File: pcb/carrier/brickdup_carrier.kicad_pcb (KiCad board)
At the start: 2 copper layers, 62 x 44 mm, 33 parts, among them J1 VBAT IN (JST PH), SW1 PWR SWITCH (JST PH), U1 MP9486A

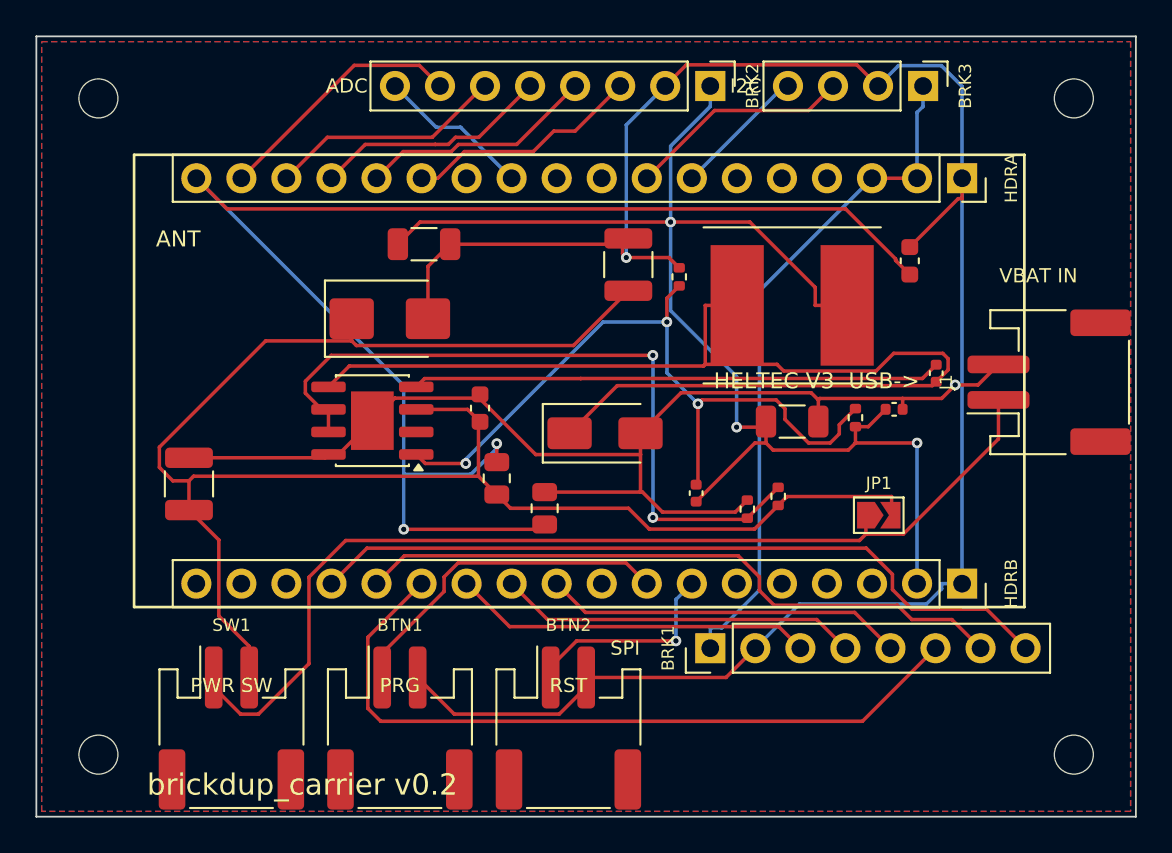
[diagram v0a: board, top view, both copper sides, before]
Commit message: pcb: widen carrier connector spacing for SMT assembly margins
Measured envelope gaps (pads+courtyard union) and widened the tight spots:
BTN1/BTN2 JST spacing 0.25mm -> 0.75mm courtyard gap, BRK1 moved 0.7mm south
of the HDRB socket. All machine-placed (SMT-SMT) pairs now >= 0.75mm; the
v0.1 D2 trouble cluster sits at D2<->D1 4.9mm / D2<->L1 13.9mm.

apply_route.py: WriteDRCReport crashes standalone; starved-thermal healing
moved to fix_thermals.py driven by kicad-cli DRC json. Final DRC: 0/0.

Co-Authored-By: Claude Fable 5 <noreply@anthropic.com>
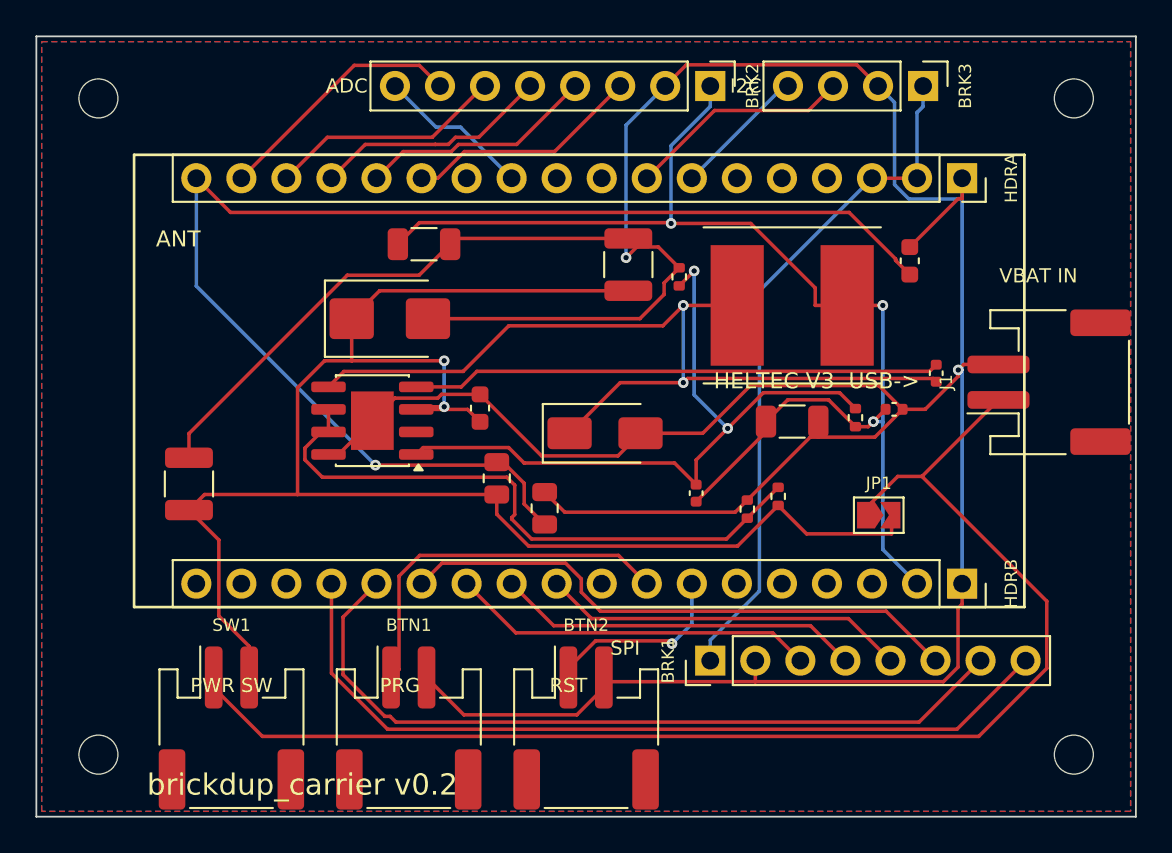
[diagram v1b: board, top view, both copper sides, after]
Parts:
- moved BTN2 1.00 mm to (31.0, 39.0)
- moved BRK1 0.70 mm to (38.0, 35.2)
- moved BTN1 0.50 mm to (21.0, 39.0)
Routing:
- net GND: track 185.0 -> 219.2 mm
- net VBATIN: track 58.0 -> 74.4 mm
- net SW: track 64.7 -> 51.3 mm, vias 0 -> 2
- net IO47: track 42.3 -> 32.2 mm
- net SENSE: track 82.4 -> 74.6 mm, vias 2 -> 1
- net +5V: track 78.2 -> 70.5 mm
- net IO48: track 37.3 -> 44.4 mm
- net EN: track 40.8 -> 34.7 mm, vias 2 -> 0
- net IO26: track 42.8 -> 47.1 mm
- net PRG: track 19.4 -> 21.0 mm
- net FB: track 41.5 -> 40.0 mm, vias 3 -> 2
- net RST: track 11.9 -> 10.9 mm
- net VBAT: track 96.9 -> 97.0 mm, vias 0 -> 2

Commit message: pcb: carrier Cff footprint 0402 -> 0603 for hand-rework
Cff is the designated bench-tuning part (hysteretic ripple injection); 0603
matches the cap kit and human hands. Re-placed + re-routed, DRC 0/0.

Co-Authored-By: Claude Fable 5 <noreply@anthropic.com>
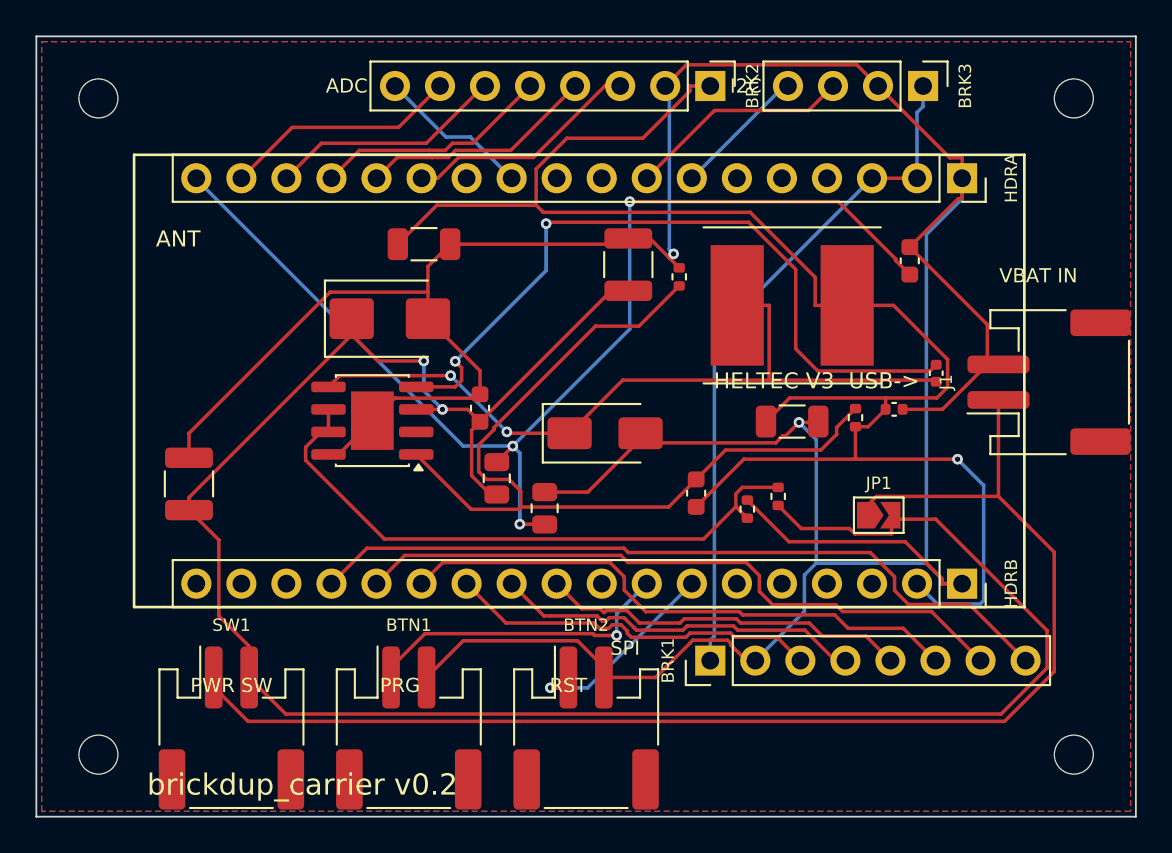
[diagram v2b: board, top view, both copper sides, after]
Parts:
- removed the Cff at (37.2, 25.8)
- added Cff: 470pF, C_0603_1608Metric, F.Cu at (37.2, 25.8)
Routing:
- net +5V: track 70.5 -> 96.4 mm, vias 3 -> 1
- net VBAT: track 97.0 -> 122.2 mm
- net GND: track 219.2 -> 203.2 mm
- net BST: track 29.8 -> 42.1 mm, vias 0 -> 2
- net SENSE: track 74.6 -> 65.4 mm, vias 1 -> 3
- net FB: track 40.0 -> 48.9 mm, vias 2 -> 0
- net SW: track 51.3 -> 43.2 mm
- net IO48: track 44.4 -> 37.7 mm
- net IO26: track 47.1 -> 43.0 mm
- net PRG: track 21.0 -> 17.7 mm, vias 0 -> 1
- net IO6: track 14.3 -> 13.4 mm
- net RST: track 10.9 -> 11.7 mm

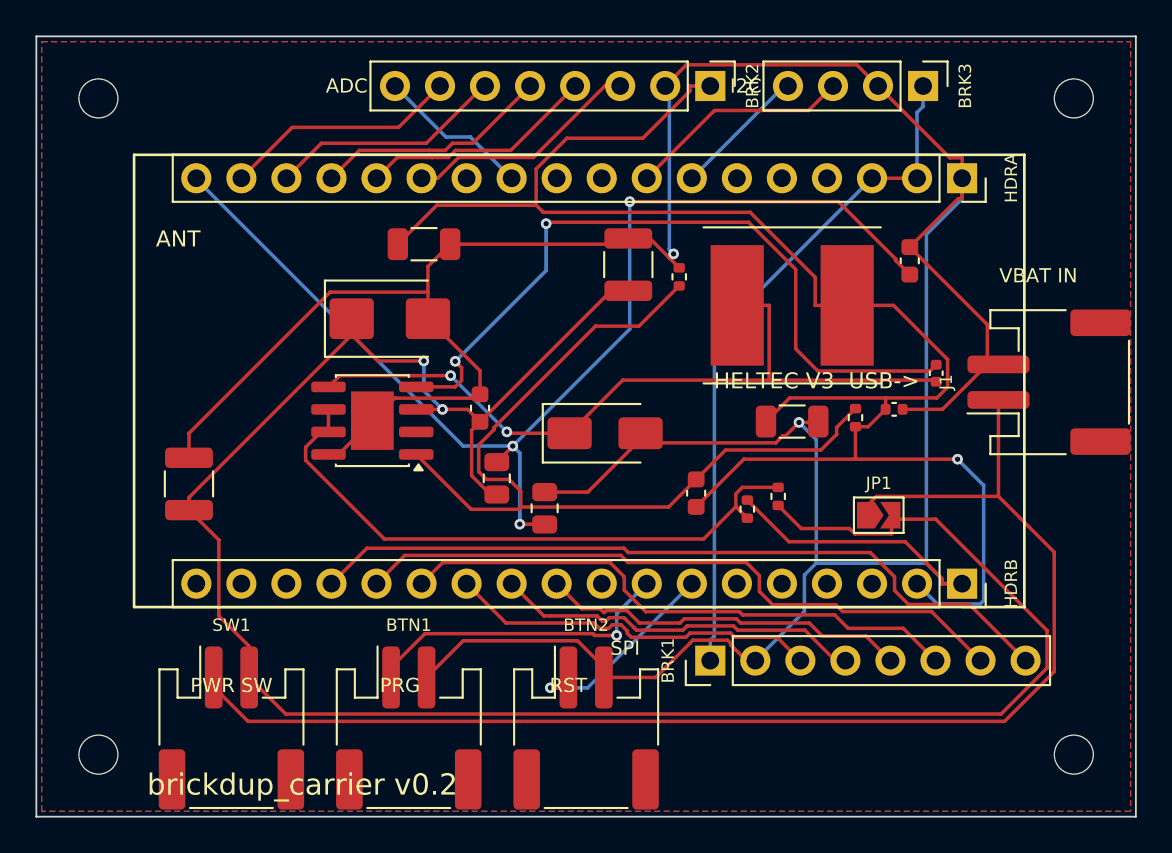
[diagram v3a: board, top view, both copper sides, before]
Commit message: pcb: pin the buck hot loop rigid (SW node 23mm -> 8mm)
Reviewing the 3D renders revealed the placement solver had scattered the
power stage (U1 SW pin, D1, L1 spread ~23mm) — the solver optimizes overlap,
not net length, violating the v0.1 "#1 EMI/stability" tight-SW-loop rule.
U1/D1/L1/Cbst are now FIXED as a hand-spaced cluster (courtyard-verified,
DRC-clean): SW triangle ~8mm, Cbst on U1's BST pin. Re-routed, DRC 0/0,
renders + layout SVGs regenerated.

Co-Authored-By: Claude Fable 5 <noreply@anthropic.com>
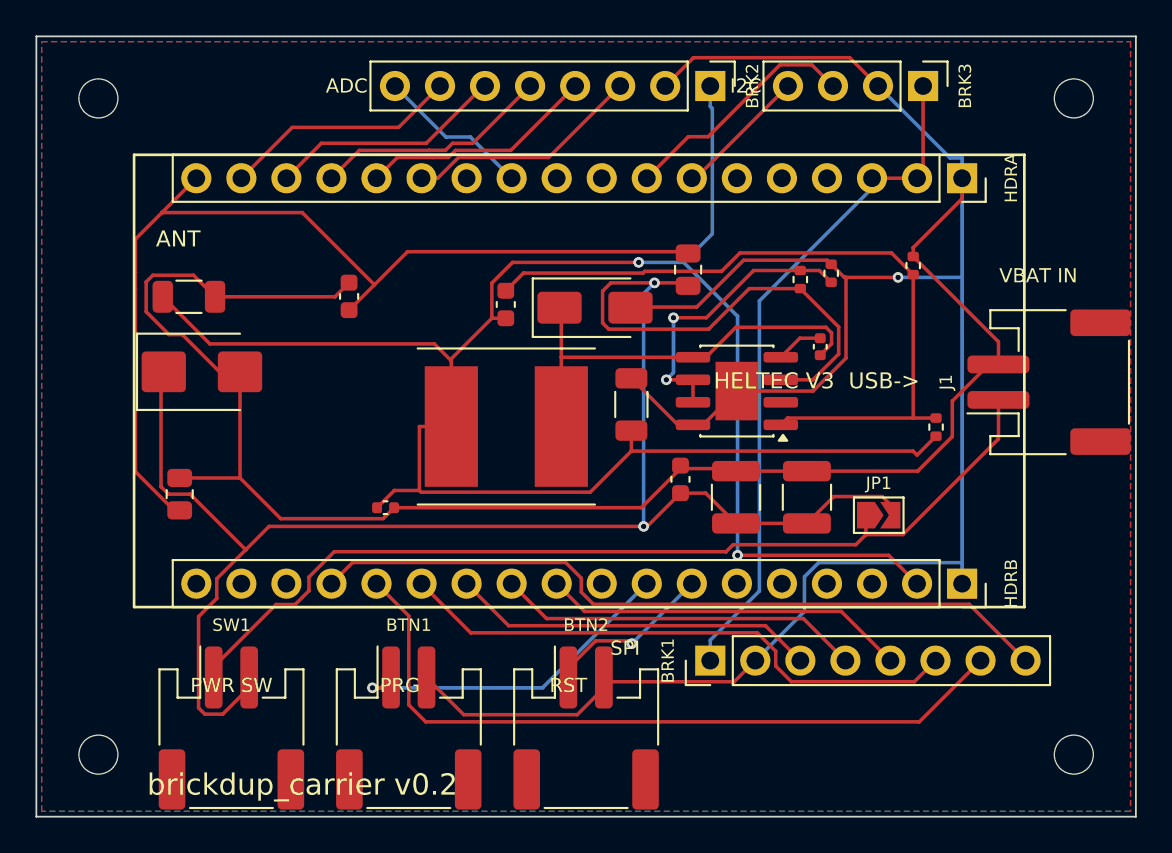
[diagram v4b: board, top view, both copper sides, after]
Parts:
- moved C1 31.7 mm to (17.6, 14.7)
- moved Cin2 30.9 mm to (39.5, 26.0)
- moved Cout3 29.2 mm to (19.7, 26.6)
- moved U1 20.6 mm to (39.5, 20.0)
- moved R2 20.6 mm to (8.08, 25.8)
- moved L1 17.5 mm to (26.5, 22.0), turned to 180 degrees
- moved Cin1 16.5 mm to (43.5, 26.0)
- moved R1 16.0 mm to (36.8, 13.2)
- moved Cff 15.1 mm to (26.5, 15.1)
- moved REN2 14.1 mm to (44.8, 13.4)
- moved Cout2 13.6 mm to (8.60, 14.7)
- moved RFB2 13.2 mm to (49.4, 12.9)
- moved REN1 12.3 mm to (43.1, 13.7)
- moved Cin3 12.0 mm to (36.3, 25.0)
- moved D2 11.0 mm to (9.33, 18.9)
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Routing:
- net BST: track 42.1 -> 2.67 mm, vias 2 -> 0
- net +5V: track 96.4 -> 118.1 mm, vias 1 -> 2
- net VBATIN: track 74.7 -> 53.9 mm
- net SW: track 43.2 -> 24.3 mm, vias 2 -> 0
- net EN: track 34.7 -> 16.7 mm, vias 0 -> 2
- net VBAT: track 122.2 -> 108.4 mm
- net SENSE: track 65.4 -> 55.6 mm, vias 3 -> 0
- net GND: track 203.2 -> 212.2 mm, vias 2 -> 1
- net FB: track 48.9 -> 41.4 mm
- net IO48: track 37.7 -> 41.7 mm
- net RST: track 11.7 -> 9.59 mm
- net PRG: track 17.7 -> 19.2 mm
- net IO41: track 12.7 -> 13.6 mm
- net IO26: track 43.0 -> 42.4 mm

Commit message: pcb: deterministic functional floorplan + executable layout rules
The relax solver (overlap-only objective, random restarts) kept scrambling
the analog grouping — divider parts strewn board-wide, FB network 9mm from
U1.FB. Retired it: every part is now hand-floorplanned in FIXED, verified by
two new pipeline gates that run on every generation:
- envelope audit in gen_pcb.py: no pad+courtyard AABB overlaps anywhere,
  nothing off-board (edge-connector mouths exempt)
- check_layout.py: electrical rules as hard failures — R1 SW hot-loop
  triangle <=10mm (8.4), R2 Cbst-to-BST <=3.5mm (2.5), R3 sense divider
  >=10mm from SW (12.8), R4 Cin3-to-VIN <=6mm (3.6)

Re-routed, DRC 0/0. Fab gerbers exported (fab/brickdup_carrier-gerbers.zip)
for pre-order JLC DFM. Renders + layout SVGs regenerated.

Co-Authored-By: Claude Fable 5 <noreply@anthropic.com>
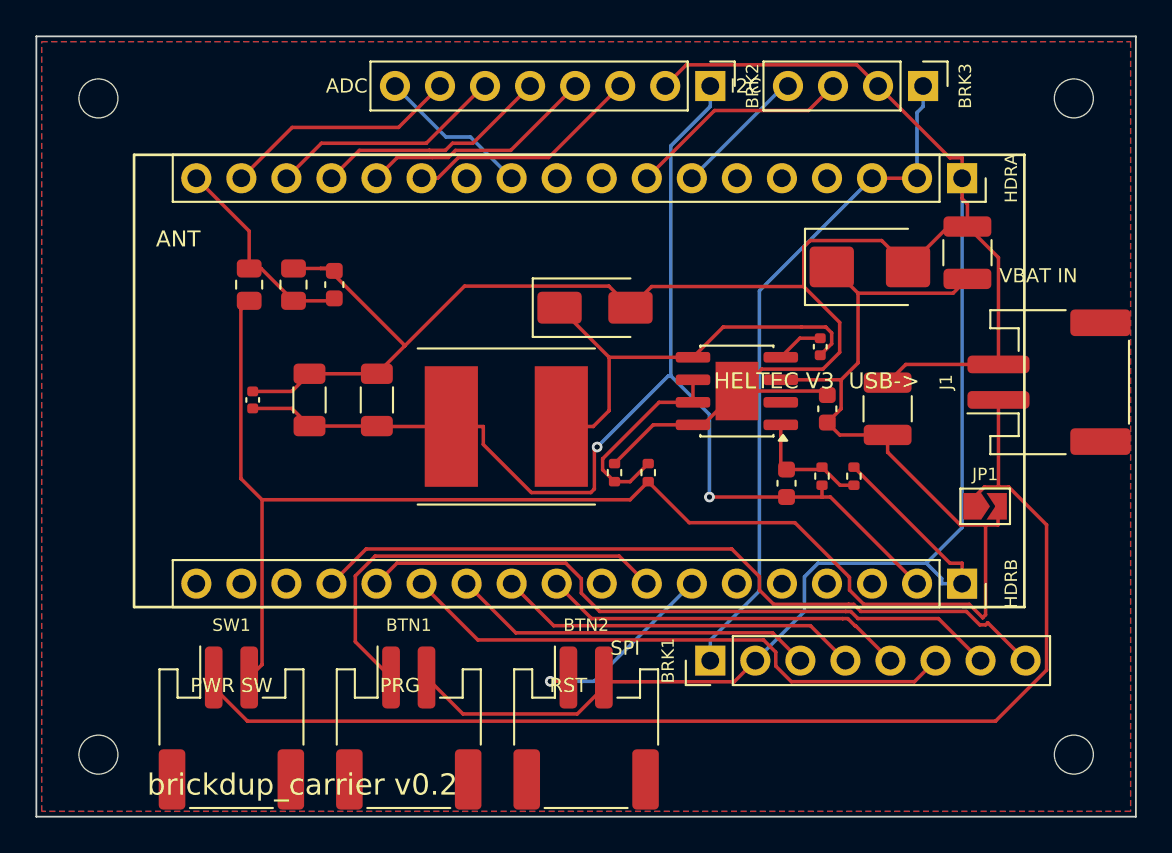
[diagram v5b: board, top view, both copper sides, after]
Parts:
- moved D2 38.1 mm to (47.0, 13.0)
- moved R1 24.8 mm to (12.0, 14.0)
- moved Cin2 19.0 mm to (52.5, 12.2)
- moved Cff 18.8 mm to (42.3, 25.2)
- moved REN2 16.6 mm to (32.6, 24.6)
- moved Cout1 14.4 mm to (19.2, 20.5)
- moved REN1 13.9 mm to (34.5, 24.6)
- moved R2 13.4 mm to (14.5, 14.0)
- moved RFB2 12.3 mm to (46.1, 24.8)
- moved Cout3 9.65 mm to (12.2, 20.5), turned to 90 degrees
- moved Cin3 9.19 mm to (44.6, 21.0)
- moved Cout2 8.95 mm to (15.4, 20.5), turned to 90 degrees
- moved RFB1 7.00 mm to (44.3, 24.8)
- moved Cin1 6.75 mm to (48.0, 21.0)
- moved JP1 6.02 mm to (53.5, 26.5)
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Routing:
- net +5V: track 118.1 -> 69.5 mm
- net SENSE: track 55.6 -> 11.9 mm
- net FB: track 41.4 -> 6.93 mm
- net GND: track 212.2 -> 188.6 mm, vias 1 -> 0
- net VBATIN: track 53.9 -> 68.4 mm
- net EN: track 16.7 -> 11.6 mm, vias 2 -> 0
- net PRG: track 19.2 -> 24.1 mm, vias 1 -> 0
- net IO48: track 41.7 -> 37.3 mm
- net VBAT: track 108.4 -> 105.8 mm, vias 2 -> 0
- net RST: track 9.59 -> 11.4 mm
- net IO41: track 13.6 -> 12.7 mm
- net IO26: track 42.4 -> 43.1 mm
- net SW: track 24.3 -> 24.9 mm

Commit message: pcb: SW1/BTN1/BTN2 -> vertical THT JST (B2B-PH-K-S, C131337)
Top-entry wire exit suits the enclosure (button wires run up to lid
flexures), THT legs are strongest for plug cycles, part is genuine JST,
in stock, and rides the same hand-solder line as the sockets. J1 stays
side-entry facing the LEMO wall. Clip access verified: >=2mm to every
neighbour (BTN2 nudged off the BRK1 row), all fully on-board (edge
exemption now J1 only). Re-routed, DRC 0/0, layout rules pass, full fab
package regenerated (gerbers/BOM/CPL).

Co-Authored-By: Claude Fable 5 <noreply@anthropic.com>
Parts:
- BTN1: value PRG BTN (JST PH) -> PRG BTN (JST PH vert); footprint JST_PH_S2B-PH-SM4-TB_1x02-1MP_P2.00mm_Horizontal -> JST_PH_B2B-PH-K_1x02_P2.00mm_Vertical
- BTN2: value RST BTN (JST PH) -> RST BTN (JST PH vert); footprint JST_PH_S2B-PH-SM4-TB_1x02-1MP_P2.00mm_Horizontal -> JST_PH_B2B-PH-K_1x02_P2.00mm_Vertical
- SW1: value PWR SWITCH (JST PH) -> PWR SWITCH (JST PH vert); footprint JST_PH_S2B-PH-SM4-TB_1x02-1MP_P2.00mm_Horizontal -> JST_PH_B2B-PH-K_1x02_P2.00mm_Vertical
- moved BTN2 1.12 mm to (30.0, 38.5)
- moved BTN1 0.50 mm to (21.0, 38.5)
- moved SW1 0.50 mm to (11.0, 38.5)
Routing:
- net +5V: track 69.5 -> 93.5 mm, vias 2 -> 1
- net PRG: track 24.1 -> 16.6 mm
- net IO26: track 43.1 -> 47.6 mm
- net VBATIN: track 68.4 -> 63.9 mm
- net IO38: track 8.73 -> 12.9 mm
- net SW: track 24.9 -> 21.8 mm
- net GND: track 188.6 -> 185.9 mm
- net BST: track 2.67 -> 4.76 mm
- net VBAT: track 105.8 -> 107.8 mm
- net RST: track 11.4 -> 10.5 mm, vias 1 -> 0
